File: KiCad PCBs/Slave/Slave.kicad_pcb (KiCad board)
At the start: 2 copper layers, 73 x 55.9 mm, 45 parts, among them J1 Screw_Terminal_01x02, J10 AVR-ISP-6, J11 Conn_01x06_Female, J12 Screw_Terminal_01x02, J13 Screw_Terminal_01x02, J14 Screw_Terminal_01x02, J15 Screw_Terminal_01x02, J16 Screw_Terminal_01x02, J2 Screw_Terminal_01x02, J3 Screw_Terminal_01x02, J4 Screw_Terminal_01x02, J5 Screw_Terminal_01x02, J6 Screw_Terminal_01x02, J7 Screw_Terminal_01x02, J8 Screw_Terminal_01x02, J9 Screw_Terminal_01x02, SW1 SW_DIP_x02, SW2 SW_DIP_x02, SW3 SW_MEC_5E, U1 ATmega328P-AU, U2 MAX487ESA+T, U3 ULN2003A, U5 AMS1117-5.0, Y1 Crystal_GND24

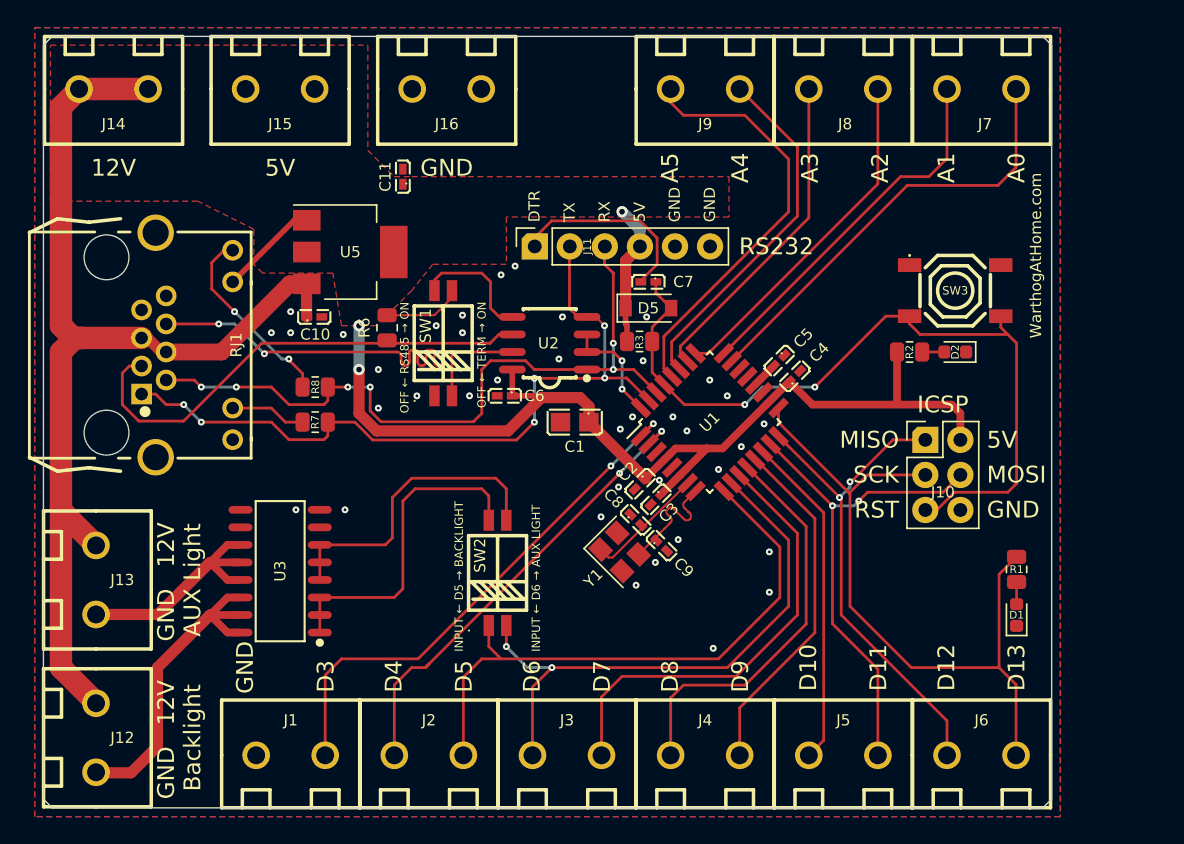
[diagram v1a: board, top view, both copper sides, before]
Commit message: Added Mounting Holes to Slave PCB Added External Connection PCB
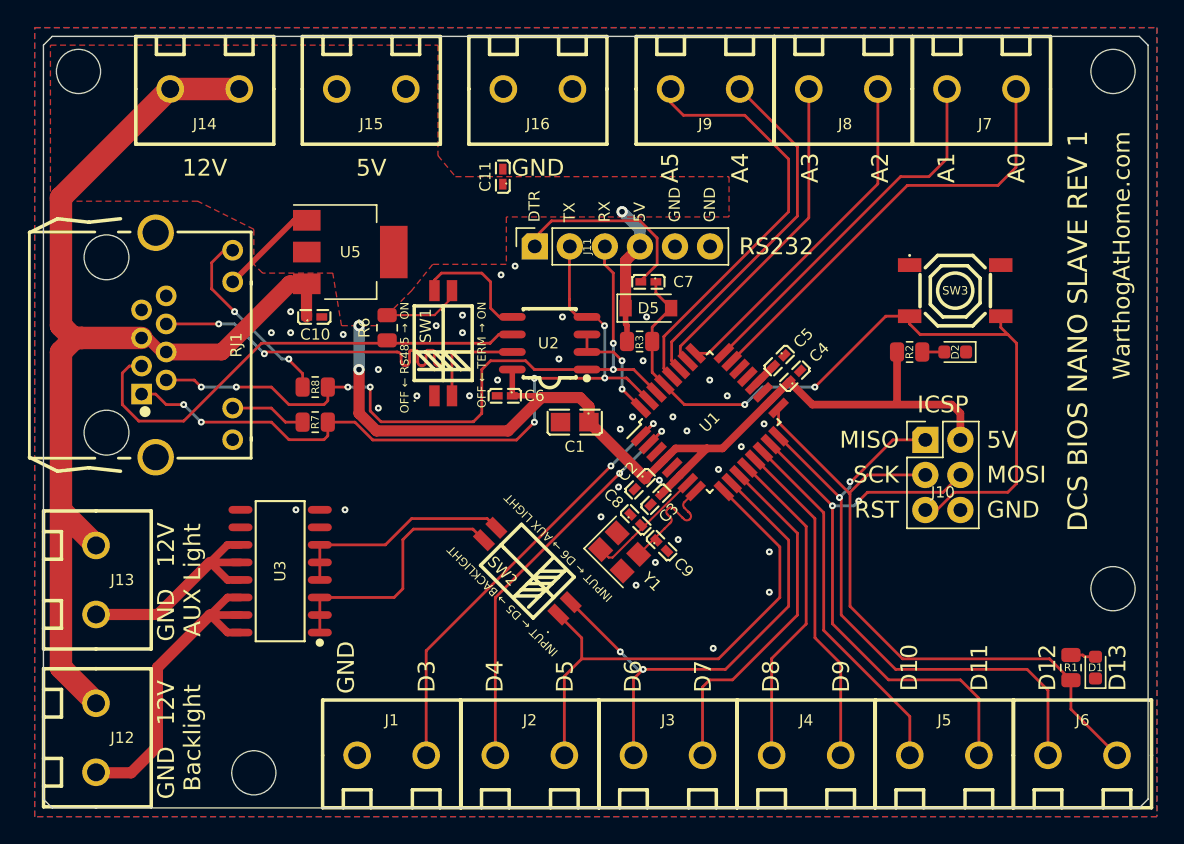
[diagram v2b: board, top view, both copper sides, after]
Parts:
- added H1: MountingHole, MountingHole:MountingHole_3.2mm_M3, F.Cu at (104.1, 78.7)
- added H2: MountingHole, MountingHole:MountingHole_3.2mm_M3, F.Cu at (179.1, 78.7)
- added H3: MountingHole, MountingHole:MountingHole_3.2mm_M3, F.Cu at (116.8, 129.5)
- added H4: MountingHole, MountingHole:MountingHole_3.2mm_M3, F.Cu at (179.1, 116.2)
- moved R1 8.13 mm to (176.0, 121.9), turned to 90 degrees
- moved J2 7.32 mm to (136.8, 128.3)
- moved J3 7.32 mm to (146.8, 128.3)
- moved J4 7.32 mm to (156.8, 128.3)
- moved J5 7.32 mm to (166.9, 128.3)
- moved J6 7.32 mm to (176.9, 128.3)
- moved J1 7.32 mm to (126.8, 128.3)
- moved C11 7.24 mm to (134.9, 86.4)
- moved D1 6.87 mm to (177.8, 121.9)
- moved J14 6.60 mm to (113.3, 80.0)
- moved J15 6.60 mm to (125.3, 80.0)
- moved J16 6.60 mm to (137.4, 80.0)
- moved SW2 2.16 mm to (136.7, 114.9), turned to 45 degrees
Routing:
- net D12: track 36.3 -> 44.9 mm
- net D7: track 32.7 -> 25.8 mm
- net D3: track 38.4 -> 32.1 mm
- net D5: track 43.1 -> 37.0 mm
- net D11: track 35.9 -> 42.0 mm
- net AUX_BASE: track 22.4 -> 16.4 mm
- net D8: track 29.3 -> 23.6 mm
- net D6: track 42.0 -> 36.8 mm
- net BACKLIGHT_BASE: track 23.8 -> 18.9 mm
- net D4: track 33.8 -> 29.8 mm
- net D13: track 50.6 -> 47.6 mm
- net +12V: track 77.9 -> 80.6 mm
- net D10: track 24.2 -> 26.4 mm
- net D9: track 25.5 -> 24.0 mm
- net Net-(D1-Pad2): track 1.24 -> 1.83 mm
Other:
- board size 73 x 55.9 mm -> 80 x 55.9 mm
- board text added: "DCS BIOS NANO SLAVE REV 1"
